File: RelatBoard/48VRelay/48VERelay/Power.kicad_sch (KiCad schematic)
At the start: 0 parts

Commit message: sys_update
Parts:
- added C10: 100nF - Ceramic, symbol Device:C_Small
- added C24: 1uF - Ceramic, symbol Device:C_Small
- added C25, C32, C33: 100nF, symbol Device:C_Small
- added C26, C27, C28, C29: 10uF, CAP_CL21_SAM, symbol 10uF Cap - Samsung:CL21A106KOQNNNE
- added C30, C31: 22uF, CAP_CL21_SAM, symbol 10uF Cap - Samsung:CL21A106KOQNNNE
- added C34, C35: 1uF, symbol Device:C_Small
- added C9: C_Small, symbol Device:C_Small
- added J1: 12, symbol Connector:Jack-DC
- added L2: 1.5uH, symbol Device:L_Small
- added R25: 10k, symbol Device:R_Small
- added R26: 680kΩ, symbol Device:R_Small
- added R27: 130kΩ, symbol Device:R_Small
- added R28: 100kΩ, symbol Device:R_Small
- added TVS1: SMBJ18A, Package_SON:WSON-6-1EP_2x2mm_P0.65mm_EP1x1.6mm, symbol Power_Protection:TVS1800DRV
- added U4: 3A 32V, C1_BEL, symbol 2026-06-05_06-35-32:C1F_3
- added U5: TPS630701RNMR, RNM0015A, symbol 2026-06-05_07-38-20:TPS630701RNMR
- added U7, U8: AP7343DQ-33W5-7, AP7343DQ-33W5-7_DIO, symbol AP7343DQ-33W5-7:AP7343DQ-33W5-7
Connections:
- new net: J1.1, TVS1.4 (IN), TVS1.5 (IN), TVS1.6 (IN), U4.1
- new net: R26.2, R27.1, U5.5 (FB)
- new net: C26.2, C27.2, R25.1
- new net: L2.1, U5.11 (L1)
- new net: L2.2, U5.9 (L2)
- new net: R25.2, U5.1 (PS_SYNC), U5.14 (EN)
- new net: C25.1, U5.3 (VAUX)
- new net: R28.2, U5.2 (PG)
- new net +12V: C10.1, C24.1, C26.1, C27.1, C28.1, C9.1, U4.2, U5.12 (VIN), U5.13 (VIN)
- new net +3V3 Eth: C34.1, U8.5 (VOUT)
- new net +3V3 MCU: C35.1, U7.5 (VOUT)
- new net +5V: C29.1, C30.1, C31.1, C32.1, C33.1, R26.1, R28.1, U5.7 (VOUT), U5.8 (VOUT), U7.1 (VIN), U7.3 (EN), U8.1 (VIN), U8.3 (EN)
- new net GND: C10.2, C24.2, C25.2, C28.2, C29.2, C30.2, C31.2, C32.2, C33.2, C34.2, C35.2, C9.2, J1.2, R27.2, TVS1.1 (GND), TVS1.2 (GND), TVS1.3 (GND), TVS1.7 (GND), U5.10 (PGND), U5.15 (VSEL), U5.4 (GND), U5.6 (FB2), U7.2 (GND), U7.4 (NC), U8.2 (GND), U8.4 (NC)
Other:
- note added: ".op"
- note added: ".tran 1u 100ms"
- note added: "12V Mains"
- note added: "3v3 Mains"
- note added: "5V Mains"

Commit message: begin pcb design
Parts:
- removed U7, U8: AP7343DQ-33W5-7, AP7343DQ-33W5-7_DIO, symbol AP7343DQ-33W5-7:AP7343DQ-33W5-7
- added U6, U8: TLV1117LV33DCYR, YDC4, symbol 2026-06-15_04-40-12:TLV1117LV33DCYR
- C10, C25, C9: footprint (none) -> Capacitor_SMD:C_0201_0603Metric
- C24, C34, C35: footprint (none) -> Capacitor_SMD:C_0805_2012Metric
- C26, C27, C28, C29: footprint CAP_CL21_SAM -> Capacitor_SMD:C_0805_2012Metric
- C30, C31: footprint CAP_CL21_SAM -> Capacitor_SMD:C_1206_3216Metric
- C32, C33: value 100nF -> 1uF; footprint (none) -> Capacitor_SMD:C_0201_0603Metric
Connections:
- net +3V3 Eth: now also U8.4 (OUT)
- net +3V3 MCU: now also U6.4 (OUT)
- net +5V: now also U6.1 (IN), U8.1 (IN)
- net GND: now also U6.2 (GND), U8.2 (GND)
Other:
- moved on the sheet: C32, C33, C34, C35

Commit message: Begin PCB layout
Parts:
- removed L2: 1.5uH, symbol Device:L_Small
- removed TVS1: SMBJ18A, Package_SON:WSON-6-1EP_2x2mm_P0.65mm_EP1x1.6mm, symbol Power_Protection:TVS1800DRV
- added L3: XFL4020-152MEC, Library:IND_XFL4020_COC-M, symbol Crystal25MHz:XFL4020-152MEC
- added U7: TVS1800DRVR, Library:DRV0006A_NV, symbol TVS18V:TVS1800DRVR
- C28, C29: footprint Capacitor_SMD:C_0805_2012Metric -> Capacitor_SMD:C_0603_1608Metric
- C30, C31: footprint Capacitor_SMD:C_1206_3216Metric -> Capacitor_SMD:C_0805_2012Metric
- J1: footprint (none) -> Connector_BarrelJack:BarrelJack_CUI_PJ-102AH_Horizontal
- R25, R26, R27, R28: footprint (none) -> Resistor_SMD:R_0603_1608Metric
- U4: footprint C1_BEL -> Fuse:Fuse_1206_3216Metric
- U5: footprint RNM0015A -> Library:RNM0015A
- U6, U8: footprint YDC4 -> Library:DCY0004A_M
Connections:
- net +3V3 Eth: now also U8.3 (TAB)
- net +3V3 MCU: now also U6.3 (TAB)
- net GND: now also U7.1 (GND), U7.2 (GND), U7.3 (GND), U7.7 (PAD)
- net at J1.1, U4.1: now also U7.4 (IN), U7.5 (IN), U7.6 (IN)
- net at U5.11 (L1): now also L3.2
- net at U5.9 (L2): now also L3.1
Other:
- moved on the sheet: C10, C24, C9, U4

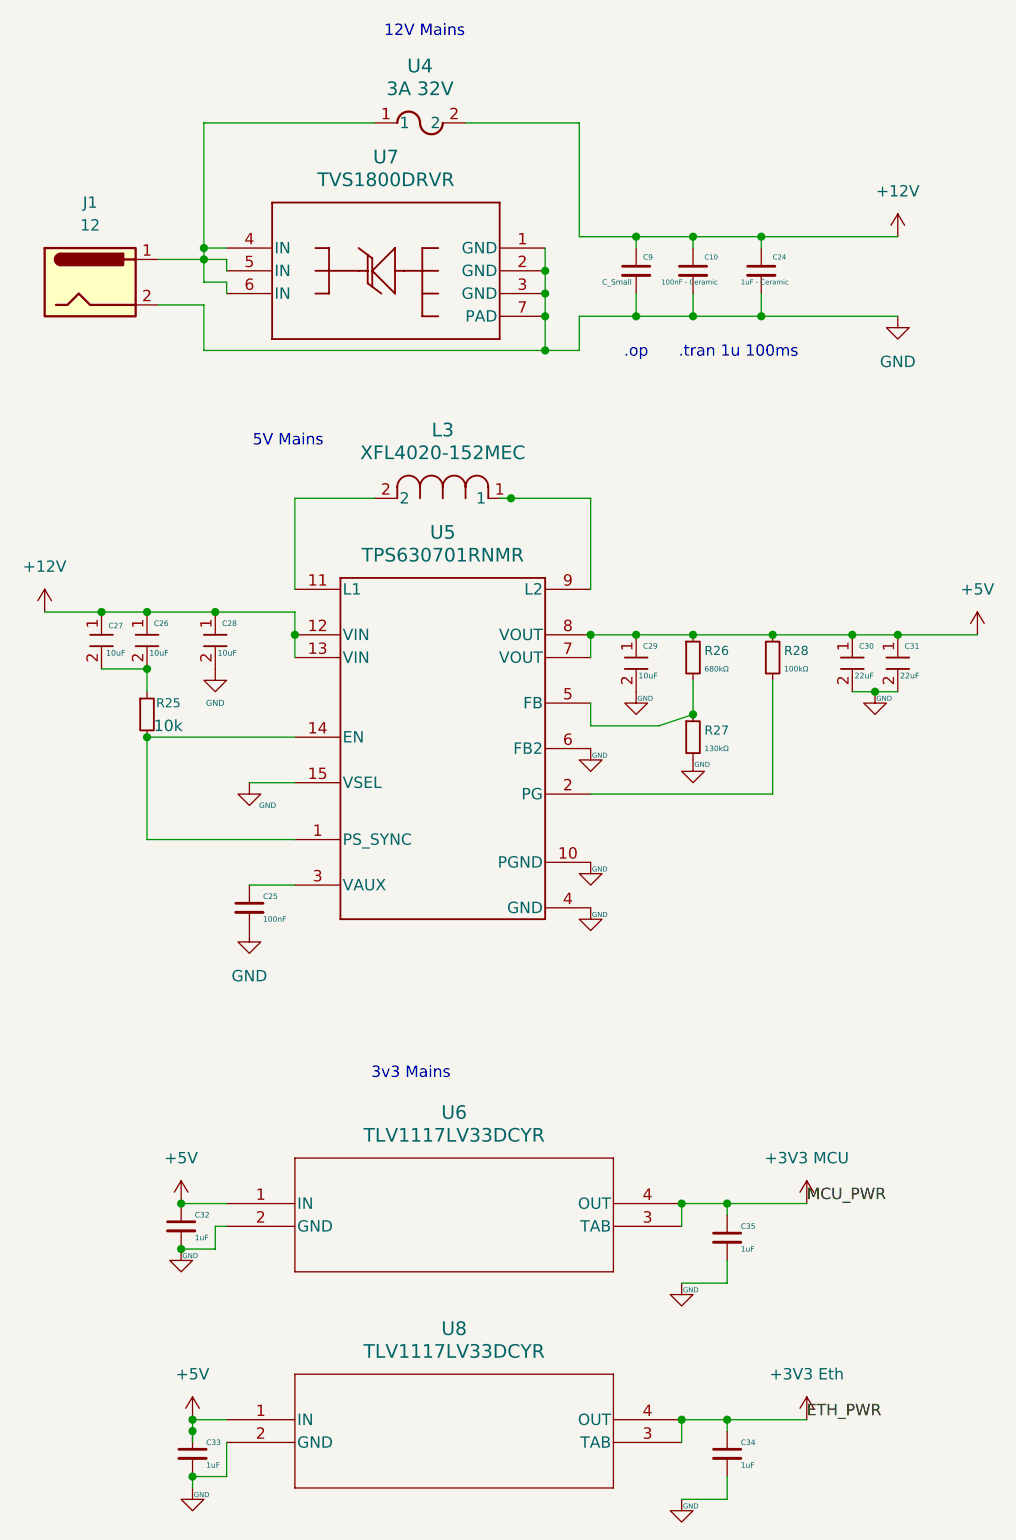
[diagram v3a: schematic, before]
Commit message: 5v5 Buck Added
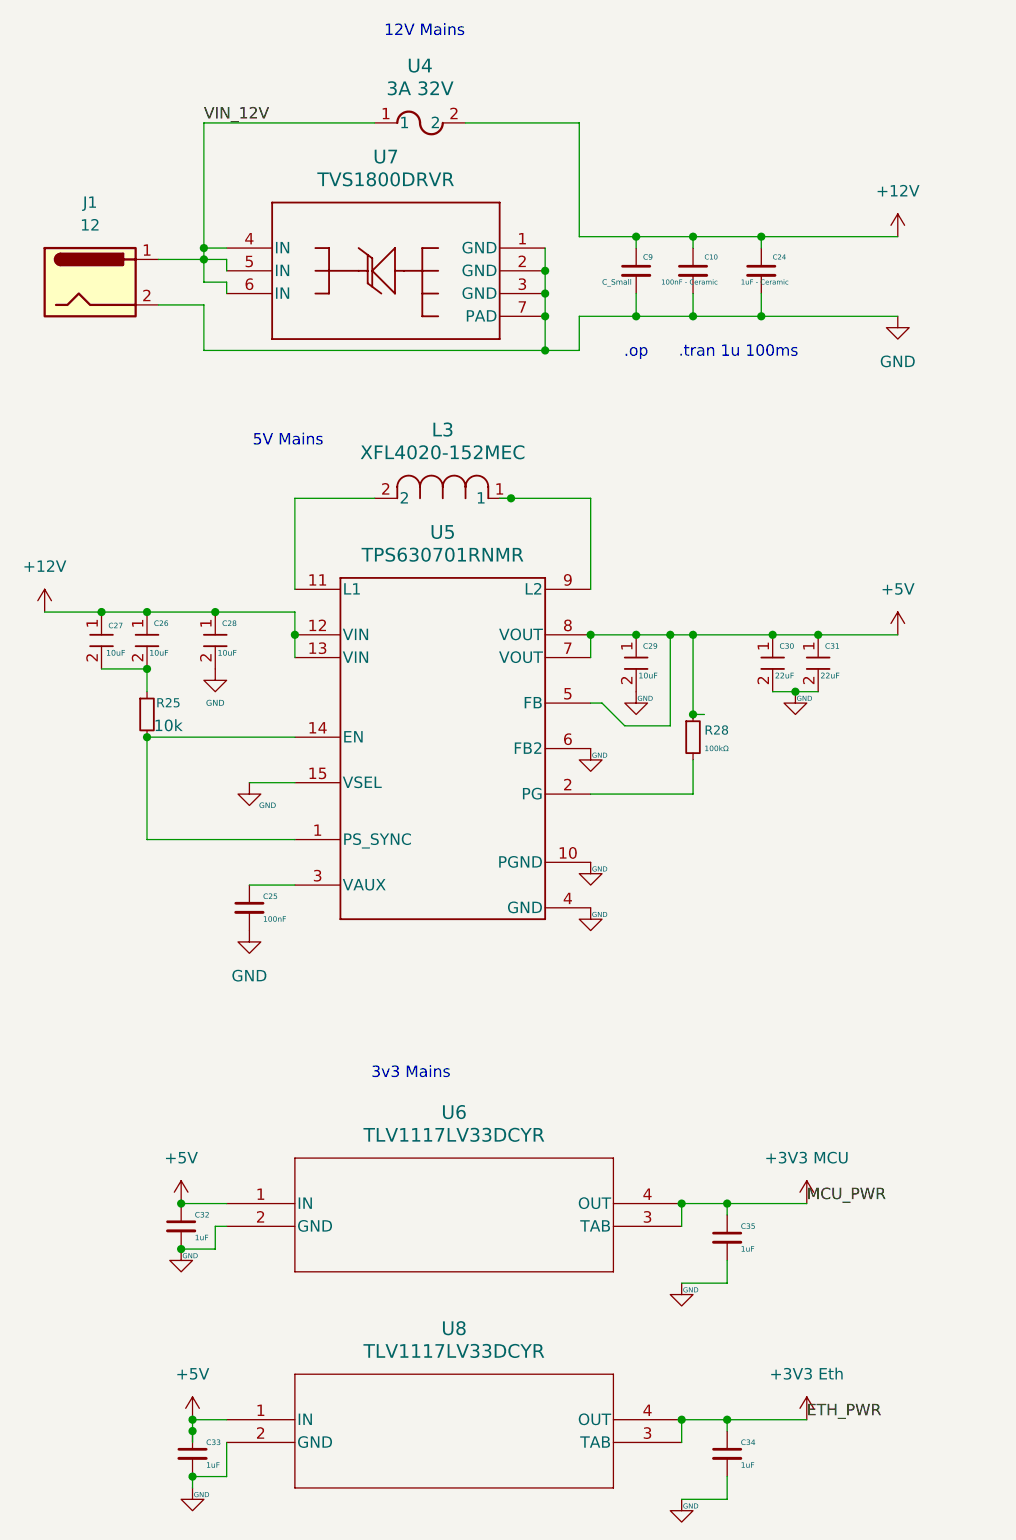
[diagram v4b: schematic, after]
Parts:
- removed R26: 680kΩ, Resistor_SMD:R_0603_1608Metric, symbol Device:R_Small
- removed R27: 130kΩ, Resistor_SMD:R_0603_1608Metric, symbol Device:R_Small
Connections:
- net +5V: now also U5.5 (FB)
- net VIN_12V: now reaches J1.1, U4.1, U7.4 (IN), U7.5 (IN), U7.6 (IN)
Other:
- moved on the sheet: C30, C31, R28

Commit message: Fix 12V->5V add power plane
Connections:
- net +12V: now also R25.1
- net GND: now also C26.2, C27.2
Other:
- moved on the sheet: R25
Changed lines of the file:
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@@
 	)
 	(junction
-		(at 113.03 90.17)
-		(diameter 0)
-		(color 0 0 0 0)
-	)
-	(junction
-		(at 52.07 92.71)
+		(at 55.88 92.71)
 		(diameter 0)
 		(color 0 0 0 0)
@@
 	)
 	(junction
+		(at 52.07 85.09)
+		(diameter 0)
+		(color 0 0 0 0)
+	)
+	(junction
 		(at 116.84 168.91)
 		(diameter 0)
@@
 	)
 	(junction
+		(at 55.88 78.74)
+		(diameter 0)
+		(color 0 0 0 0)
+	)
+	(junction
 		(at 68.58 81.28)
 		(diameter 0)
@@
 	)
 	(junction
-		(at 52.07 85.09)
-		(diameter 0)
-		(color 0 0 0 0)
-	)
-	(junction
 		(at 57.15 170.18)
 		(diameter 0)
@@
 	(wire
 		(pts
-			(xy 52.07 85.09) (xy 52.07 87.63)
+			(xy 55.88 78.74) (xy 55.88 87.63)
 		)
 		(stroke
@@
 	(wire
 		(pts
-			(xy 52.07 78.74) (xy 59.69 78.74)
+			(xy 52.07 78.74) (xy 55.88 78.74)
 		)
 		(stroke
@@
 	(wire
 		(pts
-			(xy 68.58 104.14) (xy 52.07 104.14)
+			(xy 68.58 104.14) (xy 55.88 104.14)
 		)
 		(stroke
@@
 	(wire
 		(pts
-			(xy 52.07 92.71) (xy 68.58 92.71)
+			(xy 55.88 92.71) (xy 68.58 92.71)
 		)
 		(stroke
@@
 	(wire
 		(pts
+			(xy 52.07 86.36) (xy 52.07 85.09)
+		)
+		(stroke
+			(width 0)
+			(type default)
+		)
+	)
+	(wire
+		(pts
 			(xy 135.89 36.83) (xy 120.65 36.83)
 		)
@@
 	(wire
 		(pts
-			(xy 52.07 104.14) (xy 52.07 92.71)
+			(xy 55.88 104.14) (xy 55.88 92.71)
 		)
 		(stroke
@@
 	(wire
 		(pts
-			(xy 114.3 90.17) (xy 113.03 90.17)
-		)
-		(stroke
-			(width 0)
-			(type default)
-		)
-	)
-	(wire
-		(pts
 			(xy 60.96 40.64) (xy 60.96 39.37)
 		)
@@
 		(pts
 			(xy 53.34 39.37) (xy 58.42 39.37)
+		)
+		(stroke
+			(width 0)
+			(type default)
+		)
+	)
+	(wire
+		(pts
+			(xy 55.88 78.74) (xy 59.69 78.74)
 		)
 		(stroke
@@
 	(symbol
 		(lib_id "power:GND")
+		(at 52.07 86.36 0)
+		(unit 1)
+		(body_style 1)
+		(exclude_from_sim no)
+		(in_bom yes)
+		(on_board yes)
+		(in_pos_files yes)
+		(dnp no)
+		(fields_autoplaced yes)
+		(property "Reference" "#PWR046"
+			(at 52.07 92.71 0)
+			(hide yes)
+			(show_name no)
+			(do_not_autoplace no)
+			(effects
+				(font
+					(size 1.27 1.27)
+				)
+			)
+		)
+		(property "Value" "GND"
+			(at 52.07 90.17 0)
+			(show_name no)
+			(do_not_autoplace no)
+			(effects
+				(font
+					(size 0.6604 0.6604)
+				)
+			)
+		)
+		(property "Footprint" ""
+			(at 52.07 86.36 0)
+			(hide yes)
+			(show_name no)
+			(do_not_autoplace no)
+			(effects
+				(font
+					(size 1.27 1.27)
+				)
+			)
+		)
+		(property "Datasheet" ""
+			(at 52.07 86.36 0)
+			(hide yes)
+			(show_name no)
+			(do_not_autoplace no)
+			(effects
+				(font
+					(size 1.27 1.27)
+				)
+			)
+		)
+		(property "Description" "Power symbol creates a global label with name \"GND\" , ground"
+			(at 52.07 86.36 0)
+			(hide yes)
+			(show_name no)
+			(do_not_autoplace no)
+			(effects
+				(font
+					(size 1.27 1.27)
+				)
+			)
+		)
+		(pin "1"
+		)
+		(instances
+			(project "48VERelay"
+				(path "/2d740e7a-a48e-41b8-b74e-ca0ab277f7d9/d97737bf-97d5-4dce-8e29-3da18c767258"
+					(reference "#PWR046")
+					(unit 1)
+				)
+			)
+		)
+	)
+	(symbol
+		(lib_id "power:GND")
 		(at 55.88 149.86 0)
 		(unit 1)
@@
 	(symbol
 		(lib_id "Device:R_Small")
-		(at 52.07 90.17 0)
+		(at 55.88 90.17 0)
 		(unit 1)
 		(body_style 1)
@@
 		(dnp no)
 		(property "Reference" "R25"
-			(at 53.086 88.9 0)
+			(at 56.896 88.9 0)
 			(show_name no)
 			(do_not_autoplace no)
@@
 		)
 		(property "Value" "10k"
-			(at 52.832 91.44 0)
+			(at 56.642 91.44 0)
 			(show_name no)
 			(do_not_autoplace no)
@@
 		)
 		(property "Footprint" "Resistor_SMD:R_0603_1608Metric"
-			(at 52.07 90.17 0)
+			(at 55.88 90.17 0)
 			(hide yes)
 			(show_name no)
@@
 		)
 		(property "Datasheet" ""
-			(at 52.07 90.17 0)
+			(at 55.88 90.17 0)
 			(hide yes)
 			(show_name no)
@@
 		)
 		(property "Description" "Resistor, small symbol"
-			(at 52.07 90.17 0)
-			(hide yes)
-			(show_name no)
+			(at 55.88 90.17 0)
+			(hide yes)
+			(show_name no)
